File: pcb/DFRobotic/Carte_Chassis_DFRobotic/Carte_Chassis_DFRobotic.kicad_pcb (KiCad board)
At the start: 2 copper layers, 100 x 85 mm, 52 parts, among them J1 Conn_01x03, J10 DF3A-5P-2DS, J11 DF3A-4P-2DS, J12 DF3A-4P-2DS, J13 Conn_01x02, J14 Conn_01x03, J15 Conn_01x03, J16 Conn_02x05_Odd_Even, J17 Conn_01x03, J7 Samtec FTS-105-01-L-DV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

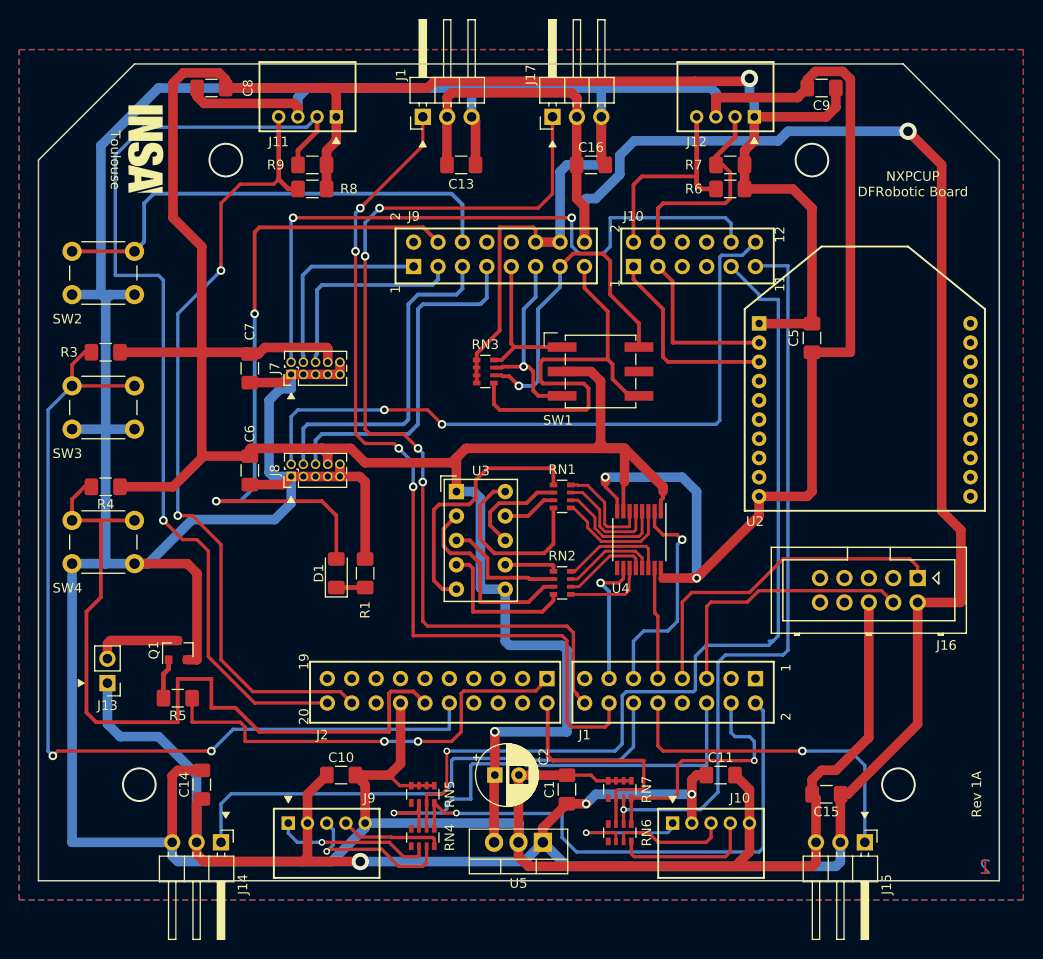
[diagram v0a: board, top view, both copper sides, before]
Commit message: Ajout des regles NXP Cup pour 2020 (V1) + modifs mineures sur pcbs
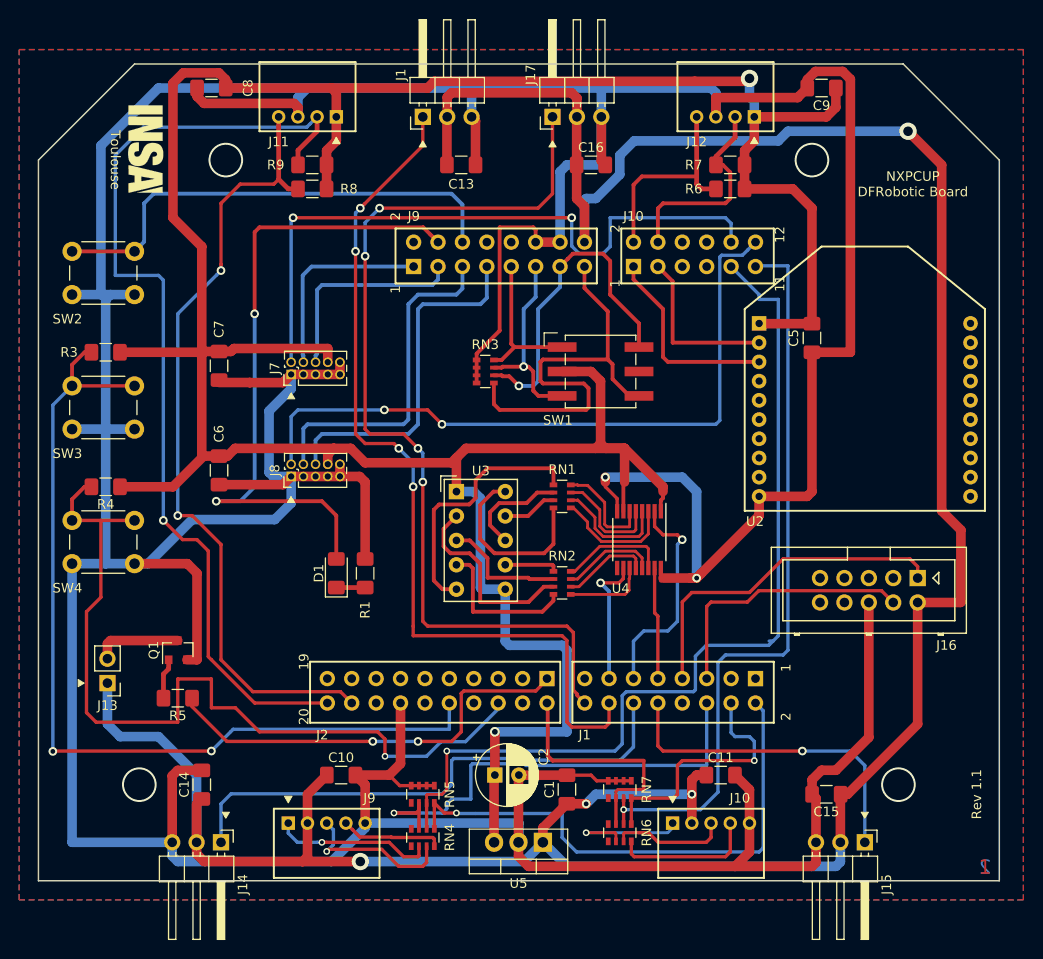
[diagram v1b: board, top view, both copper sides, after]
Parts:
- R1: value 100R -> 2.2K
- moved C7 3.21 mm to (118.8, 96.4)
- moved C6 3.20 mm to (118.8, 107.3)
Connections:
- U1 pad 2.12: /SW_USER2 -> (no net)
- U1 pad 2.6: (no net) -> /SW_USER2
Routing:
- net /SW_USER2: track 80.6 -> 88.4 mm, vias 0 -> 1
- net GND: track 609.2 -> 615.0 mm
- net /CAM_LED: track 46.3 -> 44.4 mm
- net /SW_USER1: track 96.1 -> 95.1 mm
- net +3V3: track 330.2 -> 329.6 mm
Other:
- board text added: "Rev 1.1"
- board text removed: "Rev 1A"
